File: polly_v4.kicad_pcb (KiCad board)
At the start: 2 copper layers, 68.6 x 53.3 mm, 40 parts, among them J5 Conn_02x06_Odd_Even, P1 Power, P2 Analog, P3 Digital, P4 Digital, P5 CONN_01X01, P6 CONN_01X01, P7 CONN_01X01, P8 CONN_01X01, U1 4051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

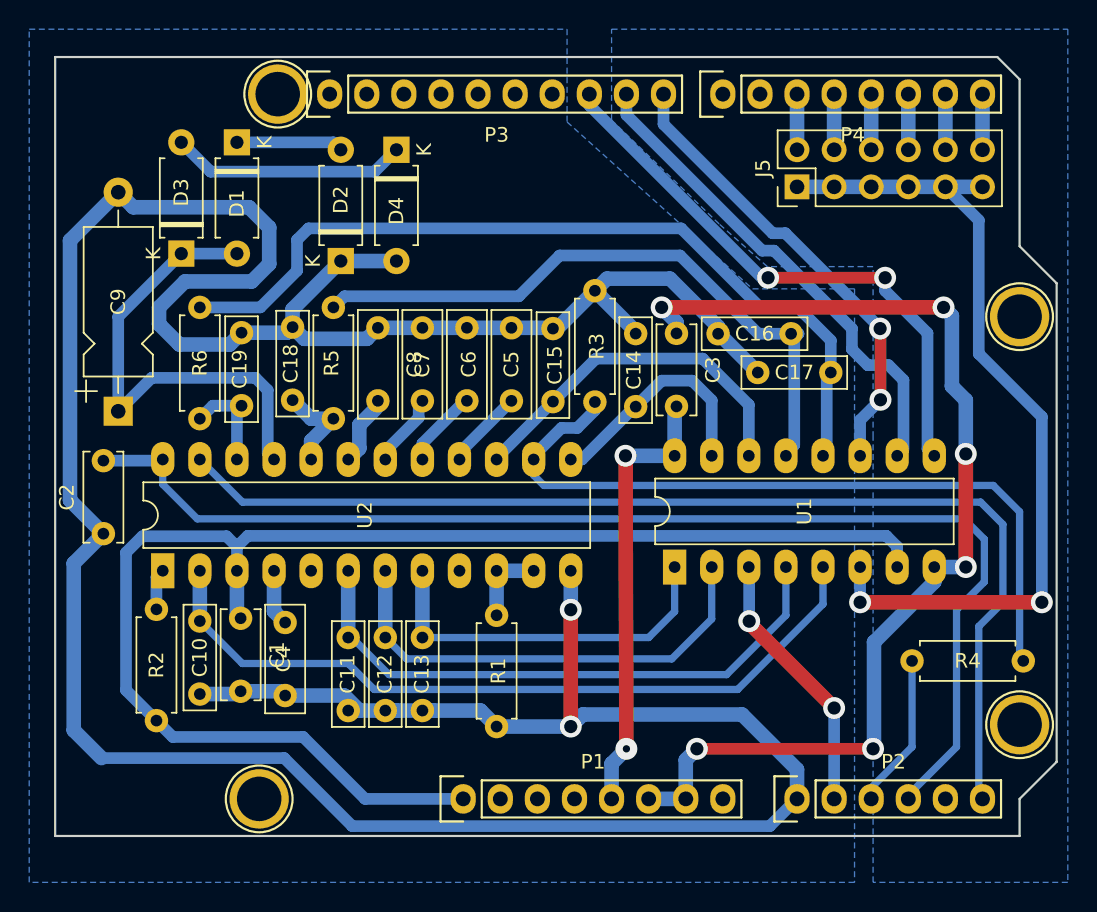
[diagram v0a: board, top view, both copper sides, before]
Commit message: Imporove layout for single sided, add previous versions
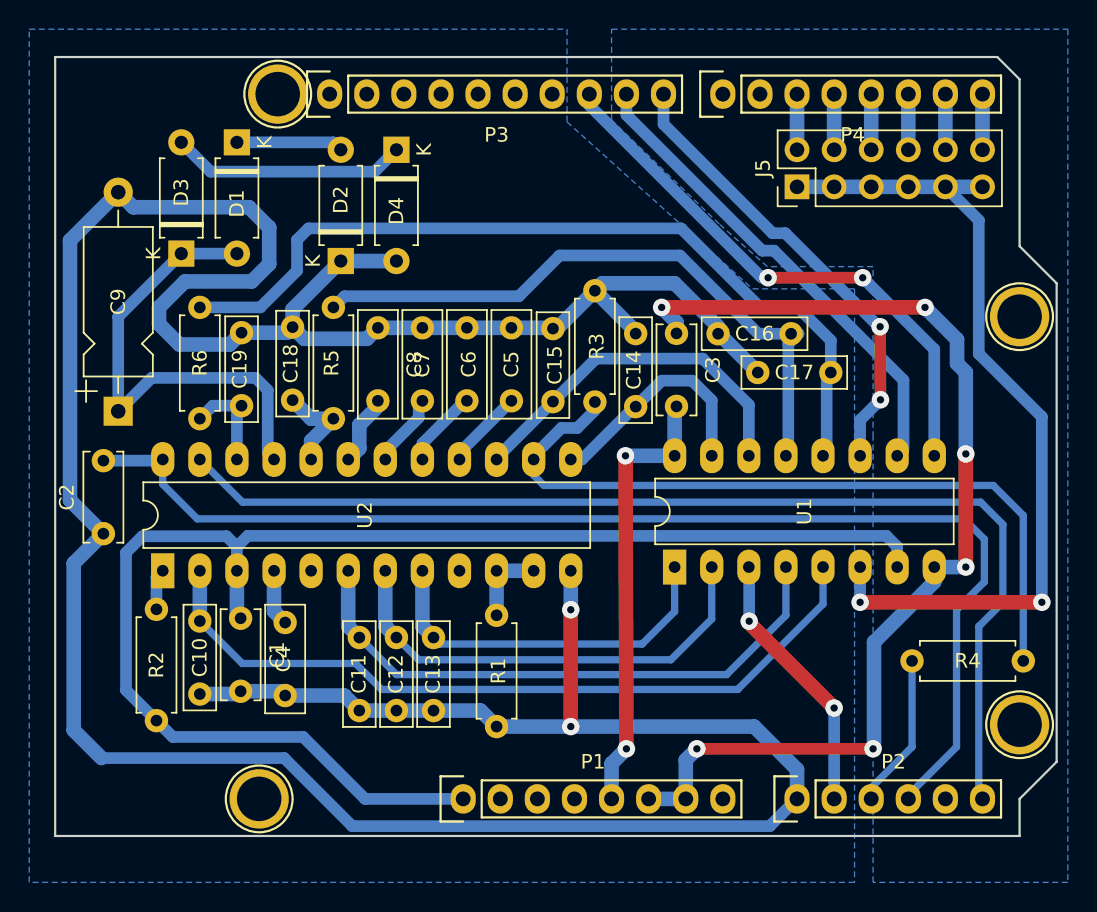
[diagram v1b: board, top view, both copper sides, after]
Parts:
- moved C11 0.76 mm to (131.8, 112.8)
- moved C12 0.76 mm to (134.4, 112.8)
- moved C13 0.76 mm to (136.9, 112.8)
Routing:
- net GNDA: track 234.5 -> 233.6 mm
- net /PARAM_SEL_A: track 39.5 -> 38.6 mm
- net /PARAM_SEL_B: track 34.1 -> 33.3 mm
- net GND: track 74.6 -> 73.9 mm
- net /MOD_AMT: track 40.8 -> 40.1 mm
